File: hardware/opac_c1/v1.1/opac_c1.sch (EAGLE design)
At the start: 68 parts, among them IC2 CP2102, IC3 ATSHA204_SOIC8, IC4 MP1584, IC5 TSC2046QFN, IC6 ATMega-328, IC7 RT9300, IC8 DS1307SO8, Q1 MMBT2222A, Q2 32.768kHz mc306, SW1 PROG, X1 8 MHz

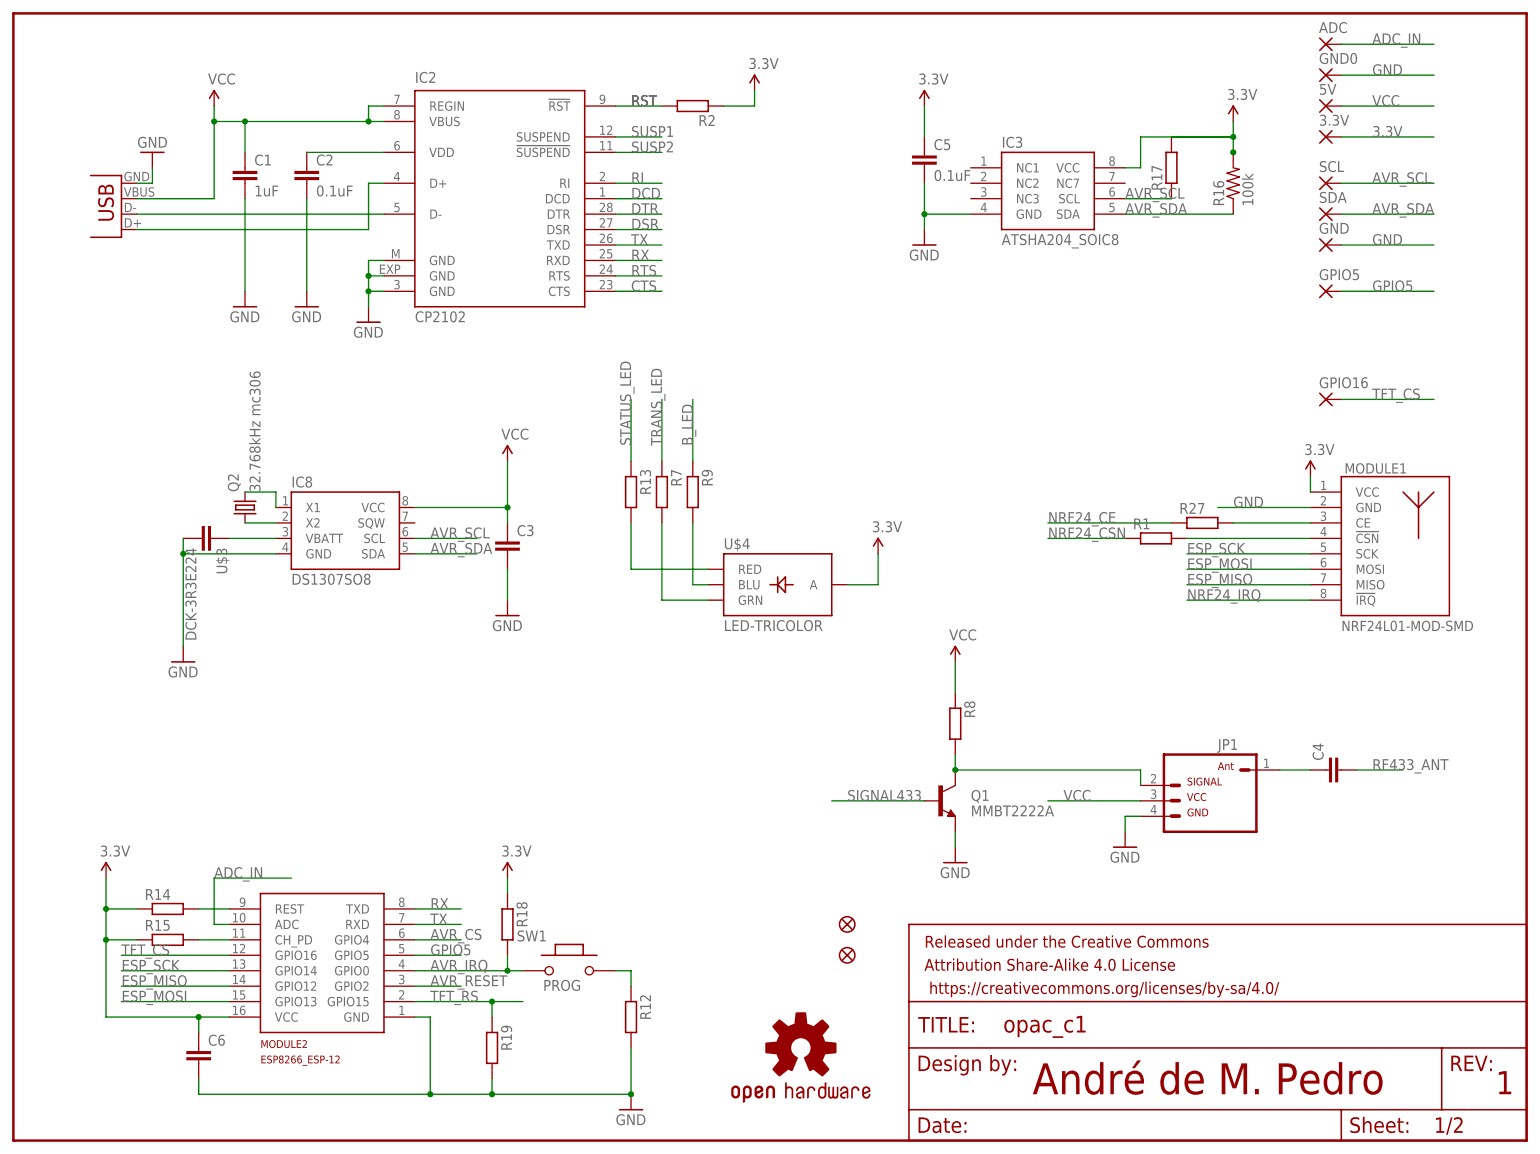
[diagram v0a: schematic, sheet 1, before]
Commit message: Several issues of the Opaq c1 hardware have been fixed.
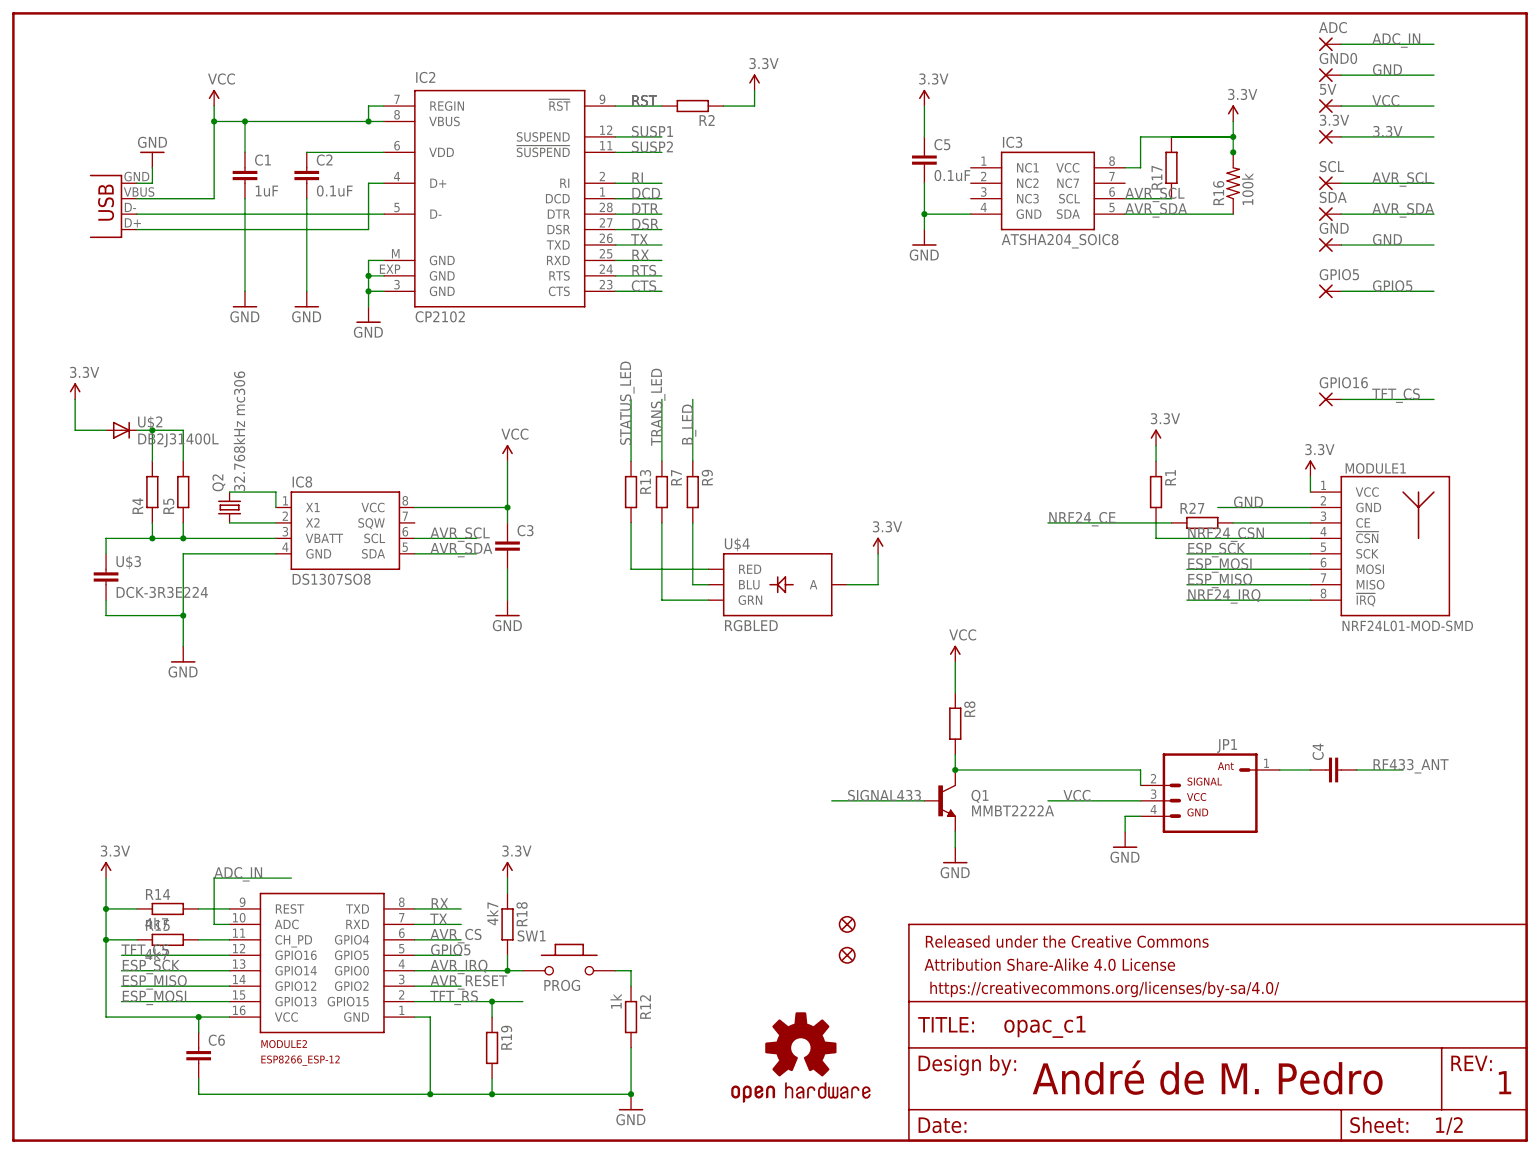
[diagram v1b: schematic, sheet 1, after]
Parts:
- added C13: (no value), resistor:C-EUC0603
- added R4, R5, R6: (no value), resistor:R-EU_R0805
- added U$2: DB2J31400L, apedro_lib:DB2J31400L
- C12: device LowPowerLab:CAP0603-CAP -> SparkFun-Passives:CAP0805
- R12: value (none) -> 1k
- R14, R15, R18: value (none) -> 4k7
- U$4: value LED-TRICOLOR -> RGBLED; device SparkFun-LED:LED-TRICOLOR -> apedro_lib:RGBLED
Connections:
- net 3.3V: now also R1.1, R6.1, U$2.A
- net AVR_CS: now also IC6.PB2(SS/OC1B); no longer IC6.PD4(XCK/T0)
- net GND: now also C13.2
- net N$1: now also R4.1, R5.1
- net N$3: now also R4.2, R5.2, U$2.C; no longer MODULE1.!CSN, R1.2
- net NRF24_CSN: now also MODULE1.!CSN, R1.2; no longer R1.1
- net TFT_DIM: now also IC6.PD3(INT1); no longer IC6.PB2(SS/OC1B)
- net TOUCH_CS: now also R6.2
- net TOUCH_IRQ: now also IC6.PD4(XCK/T0); no longer IC6.PD3(INT1)
- net VCC: now also C13.1
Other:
- moved on the sheet: Q2, R1, U$3

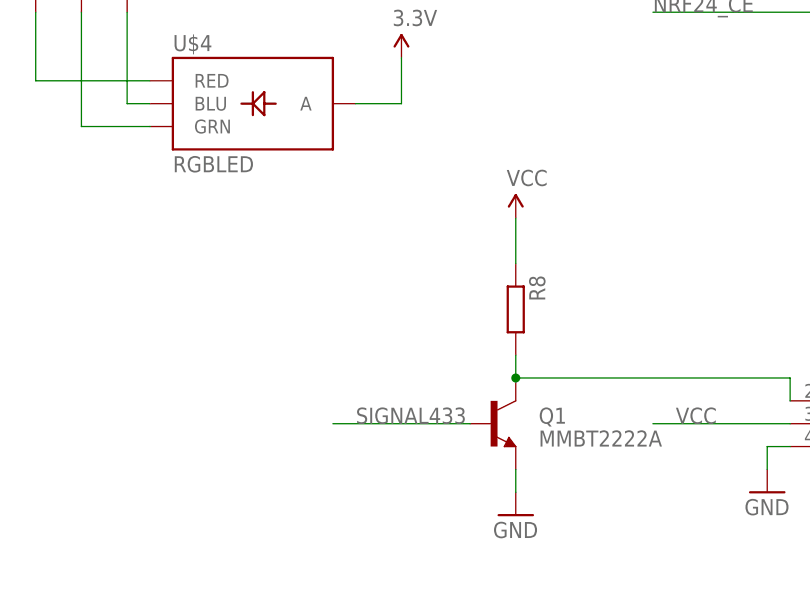
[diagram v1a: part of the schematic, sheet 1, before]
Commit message: Opaq c1 hardware has been updated.
- pull-up resistor have been added to RF433 signal.
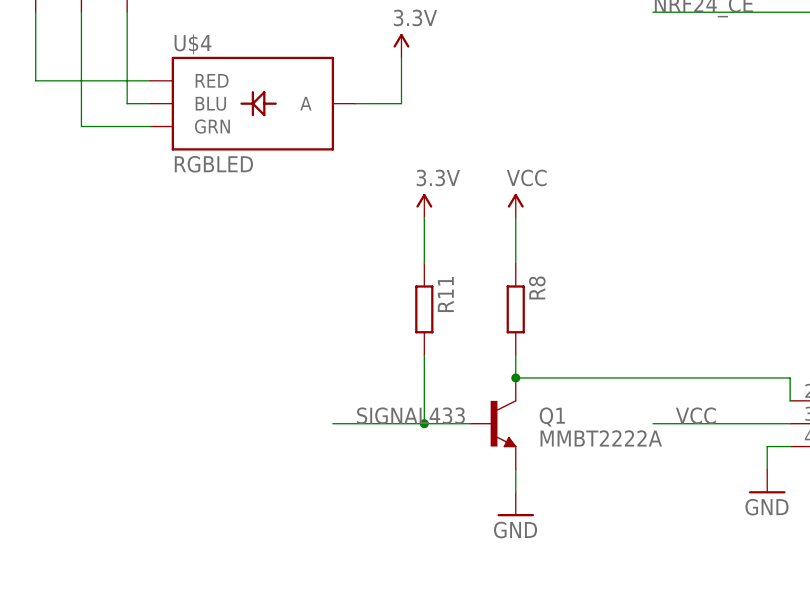
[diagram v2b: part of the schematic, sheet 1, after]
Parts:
- added R11: (no value), resistor:R-EU_R0805
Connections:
- net 3.3V: now also R11.1
- net SIGNAL433: now also R11.2
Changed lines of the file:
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@@
 <part name="P+20" library="SparkFun" deviceset="3.3V" device=""/>
 <part name="R6" library="resistor" deviceset="R-EU_" device="R0805"/>
+<part name="R11" library="resistor" deviceset="R-EU_" device="R0805"/>
+<part name="P+21" library="SparkFun" deviceset="3.3V" device=""/>
 </parts>
 <sheets>
@@
 <instance part="P+19" gate="G$1" x="10.16" y="121.92"/>
 <instance part="U$2" gate="G$1" x="17.78" y="116.84"/>
+<instance part="R11" gate="G$1" x="144.78" y="68.58" rot="R270"/>
+<instance part="P+21" gate="G$1" x="144.78" y="78.74"/>
 </instances>
 <busses>
@@
 <wire x1="10.16" y1="116.84" x2="15.24" y2="116.84" width="0.1524" layer="91"/>
 </segment>
+<segment>
+<pinref part="R11" gate="G$1" pin="1"/>
+<pinref part="P+21" gate="G$1" pin="3.3V"/>
+<wire x1="144.78" y1="73.66" x2="144.78" y2="78.74" width="0.1524" layer="91"/>
+</segment>
 </net>
 <net name="GND" class="0">
@@
 <segment>
 <pinref part="Q1" gate="G$1" pin="B"/>
-<wire x1="149.86" y1="55.88" x2="134.62" y2="55.88" width="0.1524" layer="91"/>
+<wire x1="149.86" y1="55.88" x2="144.78" y2="55.88" width="0.1524" layer="91"/>
 <label x="137.16" y="55.88" size="1.778" layer="95"/>
-</segment>
-</net>
+<pinref part="R11" gate="G$1" pin="2"/>
+<wire x1="144.78" y1="55.88" x2="134.62" y2="55.88" width="0.1524" layer="91"/>
+<wire x1="144.78" y1="63.5" x2="144.78" y2="55.88" width="0.1524" layer="91"/>
+<junction x="144.78" y="55.88"/>
+</segment>
+</net>

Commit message: Added the new fixes for opaq c1 hardware.
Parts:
- added ADC6: TPTP09R, testpad:TPTP09R
- added RX, TX: TPTP10SQ, testpad:TPTP10SQ
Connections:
- net A6: now also ADC6.TP
- net D0_RX: now also RX.TP
- net D1_TX: now also TX.TP
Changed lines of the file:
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@@
 <grid distance="0.1" unitdist="inch" unit="inch" style="lines" multiple="1" display="no" altdistance="0.01" altunitdist="inch" altunit="inch"/>
 <layers>
-<layer number="1" name="Top" color="4" fill="1" visible="yes" active="no"/>
-<layer number="2" name="Route2" color="1" fill="3" visible="yes" active="no"/>
-<layer number="3" name="Route3" color="4" fill="3" visible="yes" active="no"/>
-<layer number="4" name="Route4" color="1" fill="4" visible="yes" active="no"/>
-<layer number="5" name="Route5" color="4" fill="4" visible="yes" active="no"/>
-<layer number="6" name="Route6" color="1" fill="8" visible="yes" active="no"/>
-<layer number="7" name="Route7" color="4" fill="8" visible="yes" active="no"/>
-<layer number="8" name="Route8" color="1" fill="2" visible="yes" active="no"/>
-<layer number="9" name="Route9" color="4" fill="2" visible="yes" active="no"/>
-<layer number="10" name="Route10" color="1" fill="7" visible="yes" active="no"/>
-<layer number="11" name="Route11" color="4" fill="7" visible="yes" active="no"/>
-<layer number="12" name="Route12" color="1" fill="5" visible="yes" active="no"/>
-<layer number="13" name="Route13" color="4" fill="5" visible="yes" active="no"/>
-<layer number="14" name="Route14" color="1" fill="6" visible="yes" active="no"/>
-<layer number="15" name="Route15" color="4" fill="6" visible="yes" active="no"/>
-<layer number="16" name="Bottom" color="1" fill="1" visible="yes" active="no"/>
-<layer number="17" name="Pads" color="2" fill="1" visible="yes" active="no"/>
-<layer number="18" name="Vias" color="2" fill="1" visible="yes" active="no"/>
-<layer number="19" name="Unrouted" color="6" fill="1" visible="yes" active="no"/>
-<layer number="20" name="Dimension" color="15" fill="1" visible="yes" active="no"/>
-<layer number="21" name="tPlace" color="7" fill="1" visible="yes" active="no"/>
-<layer number="22" name="bPlace" color="7" fill="1" visible="yes" active="no"/>
-<layer number="23" name="tOrigins" color="15" fill="1" visible="yes" active="no"/>
-<layer number="24" name="bOrigins" color="15" fill="1" visible="yes" active="no"/>
-<layer number="25" name="tNames" color="7" fill="1" visible="yes" active="no"/>
-<layer number="26" name="bNames" color="7" fill="1" visible="yes" active="no"/>
-<layer number="27" name="tValues" color="7" fill="1" visible="yes" active="no"/>
-<layer number="28" name="bValues" color="7" fill="1" visible="yes" active="no"/>
+<layer number="1" name="Top" color="4" fill="1" visible="no" active="no"/>
+<layer number="2" name="Route2" color="1" fill="3" visible="no" active="no"/>
+<layer number="3" name="Route3" color="4" fill="3" visible="no" active="no"/>
+<layer number="4" name="Route4" color="1" fill="4" visible="no" active="no"/>
+<layer number="5" name="Route5" color="4" fill="4" visible="no" active="no"/>
+<layer number="6" name="Route6" color="1" fill="8" visible="no" active="no"/>
+<layer number="7" name="Route7" color="4" fill="8" visible="no" active="no"/>
+<layer number="8" name="Route8" color="1" fill="2" visible="no" active="no"/>
+<layer number="9" name="Route9" color="4" fill="2" visible="no" active="no"/>
+<layer number="10" name="Route10" color="1" fill="7" visible="no" active="no"/>
+<layer number="11" name="Route11" color="4" fill="7" visible="no" active="no"/>
+<layer number="12" name="Route12" color="1" fill="5" visible="no" active="no"/>
+<layer number="13" name="Route13" color="4" fill="5" visible="no" active="no"/>
+<layer number="14" name="Route14" color="1" fill="6" visible="no" active="no"/>
+<layer number="15" name="Route15" color="4" fill="6" visible="no" active="no"/>
+<layer number="16" name="Bottom" color="1" fill="1" visible="no" active="no"/>
+<layer number="17" name="Pads" color="2" fill="1" visible="no" active="no"/>
+<layer number="18" name="Vias" color="2" fill="1" visible="no" active="no"/>
+<layer number="19" name="Unrouted" color="6" fill="1" visible="no" active="no"/>
+<layer number="20" name="Dimension" color="15" fill="1" visible="no" active="no"/>
+<layer number="21" name="tPlace" color="7" fill="1" visible="no" active="no"/>
+<layer number="22" name="bPlace" color="7" fill="1" visible="no" active="no"/>
+<layer number="23" name="tOrigins" color="15" fill="1" visible="no" active="no"/>
+<layer number="24" name="bOrigins" color="15" fill="1" visible="no" active="no"/>
+<layer number="25" name="tNames" color="7" fill="1" visible="no" active="no"/>
+<layer number="26" name="bNames" color="7" fill="1" visible="no" active="no"/>
+<layer number="27" name="tValues" color="7" fill="1" visible="no" active="no"/>
+<layer number="28" name="bValues" color="7" fill="1" visible="no" active="no"/>
 <layer number="29" name="tStop" color="7" fill="3" visible="no" active="no"/>
 <layer number="30" name="bStop" color="7" fill="6" visible="no" active="no"/>
@@
 <layer number="35" name="tGlue" color="7" fill="4" visible="no" active="no"/>
 <layer number="36" name="bGlue" color="7" fill="5" visible="no" active="no"/>
-<layer number="37" name="tTest" color="7" fill="1" visible="yes" active="no"/>
-<layer number="38" name="bTest" color="7" fill="1" visible="yes" active="no"/>
+<layer number="37" name="tTest" color="7" fill="1" visible="no" active="no"/>
+<layer number="38" name="bTest" color="7" fill="1" visible="no" active="no"/>
 <layer number="39" name="tKeepout" color="4" fill="11" visible="no" active="no"/>
 <layer number="40" name="bKeepout" color="1" fill="11" visible="no" active="no"/>
@@
 <layer number="44" name="Drills" color="7" fill="1" visible="no" active="no"/>
 <layer number="45" name="Holes" color="7" fill="1" visible="no" active="no"/>
-<layer number="46" name="Milling" color="3" fill="1" visible="yes" active="no"/>
-<layer number="47" name="Measures" color="7" fill="1" visible="yes" active="no"/>
-<layer number="48" name="Document" color="7" fill="1" visible="yes" active="no"/>
-<layer number="49" name="Reference" color="7" fill="1" visible="yes" active="no"/>
-<layer number="50" name="dxf" color="7" fill="1" visible="yes" active="no"/>
-<layer number="51" name="tDocu" color="7" fill="1" visible="yes" active="no"/>
-<layer number="52" name="bDocu" color="7" fill="1" visible="yes" active="no"/>
-<layer number="53" name="tGND_GNDA" color="7" fill="9" visible="yes" active="no"/>
-<layer number="54" name="bGND_GNDA" color="1" fill="9" visible="yes" active="no"/>
-<layer number="56" name="wert" color="7" fill="1" visible="yes" active="no"/>
-<layer number="57" name="tCAD" color="7" fill="1" visible="yes" active="no"/>
-<layer number="59" name="tCarbon" color="7" fill="1" visible="yes" active="no"/>
-<layer number="60" name="bCarbon" color="7" fill="1" visible="yes" active="no"/>
+<layer number="46" name="Milling" color="3" fill="1" visible="no" active="no"/>
+<layer number="47" name="Measures" color="7" fill="1" visible="no" active="no"/>
+<layer number="48" name="Document" color="7" fill="1" visible="no" active="no"/>
+<layer number="49" name="Reference" color="7" fill="1" visible="no" active="no"/>
+<layer number="50" name="dxf" color="7" fill="1" visible="no" active="no"/>
+<layer number="51" name="tDocu" color="7" fill="1" visible="no" active="no"/>
+<layer number="52" name="bDocu" color="7" fill="1" visible="no" active="no"/>
+<layer number="53" name="tGND_GNDA" color="7" fill="9" visible="no" active="no"/>
+<layer number="54" name="bGND_GNDA" color="1" fill="9" visible="no" active="no"/>
+<layer number="56" name="wert" color="7" fill="1" visible="no" active="no"/>
+<layer number="57" name="tCAD" color="7" fill="1" visible="no" active="no"/>
+<layer number="59" name="tCarbon" color="7" fill="1" visible="no" active="no"/>
+<layer number="60" name="bCarbon" color="7" fill="1" visible="no" active="no"/>
 <layer number="90" name="Modules" color="5" fill="1" visible="yes" active="yes"/>
 <layer number="91" name="Nets" color="2" fill="1" visible="yes" active="yes"/>
@@
 <part name="R11" library="resistor" deviceset="R-EU_" device="R0805"/>
 <part name="P+21" library="SparkFun" deviceset="3.3V" device=""/>
+<part name="TX" library="testpad" deviceset="TP" device="TP10SQ"/>
+<part name="RX" library="testpad" deviceset="TP" device="TP10SQ"/>
+<part name="ADC6" library="testpad" deviceset="TP" device="TP09R" value="TPTP09R"/>
 </parts>
 <sheets>
@@
 <instance part="P+20" gate="G$1" x="12.7" y="86.36"/>
 <instance part="R6" gate="G$1" x="12.7" y="78.74" rot="R270"/>
+<instance part="TX" gate="G$1" x="129.54" y="121.92"/>
+<instance part="RX" gate="G$1" x="137.16" y="121.92"/>
+<instance part="ADC6" gate="G$1" x="144.78" y="121.92"/>
 </instances>
 <busses>
@@
 <pinref part="IC6" gate="G$1" pin="PD1(TXD)"/>
 </segment>
+<segment>
+<pinref part="TX" gate="G$1" pin="TP"/>
+<wire x1="129.54" y1="119.38" x2="129.54" y2="111.76" width="0.1524" layer="91"/>
+<label x="129.54" y="111.76" size="1.778" layer="95" rot="R90"/>
+</segment>
 </net>
 <net name="D0_RX" class="0">
@@
 <pinref part="IC6" gate="G$1" pin="PD0(RXD)"/>
 </segment>
+<segment>
+<pinref part="RX" gate="G$1" pin="TP"/>
+<wire x1="137.16" y1="119.38" x2="137.16" y2="111.76" width="0.1524" layer="91"/>
+<label x="137.16" y="111.76" size="1.778" layer="95" rot="R90"/>
+</segment>
 </net>
 <net name="A7" class="0">
@@
 <pinref part="IC6" gate="G$1" pin="ADC6"/>
 </segment>
-</net>
+<segment>
+<pinref part="ADC6" gate="G$1" pin="TP"/>
+<wire x1="144.78" y1="119.38" x2="144.78" y2="111.76" width="0.1524" layer="91"/>
+<label x="144.78" y="111.76" size="1.778" layer="95" rot="R90"/>
+</segment>
+</net>
